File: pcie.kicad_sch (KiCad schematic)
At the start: 30 parts, among them J10 OCuLink_x4_Amphenol_G14A42121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, J11 OCuLink_x4_Amphenol_G14A42121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, J17 PinHeader_2x10_P1.27mm_SMD_Sh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

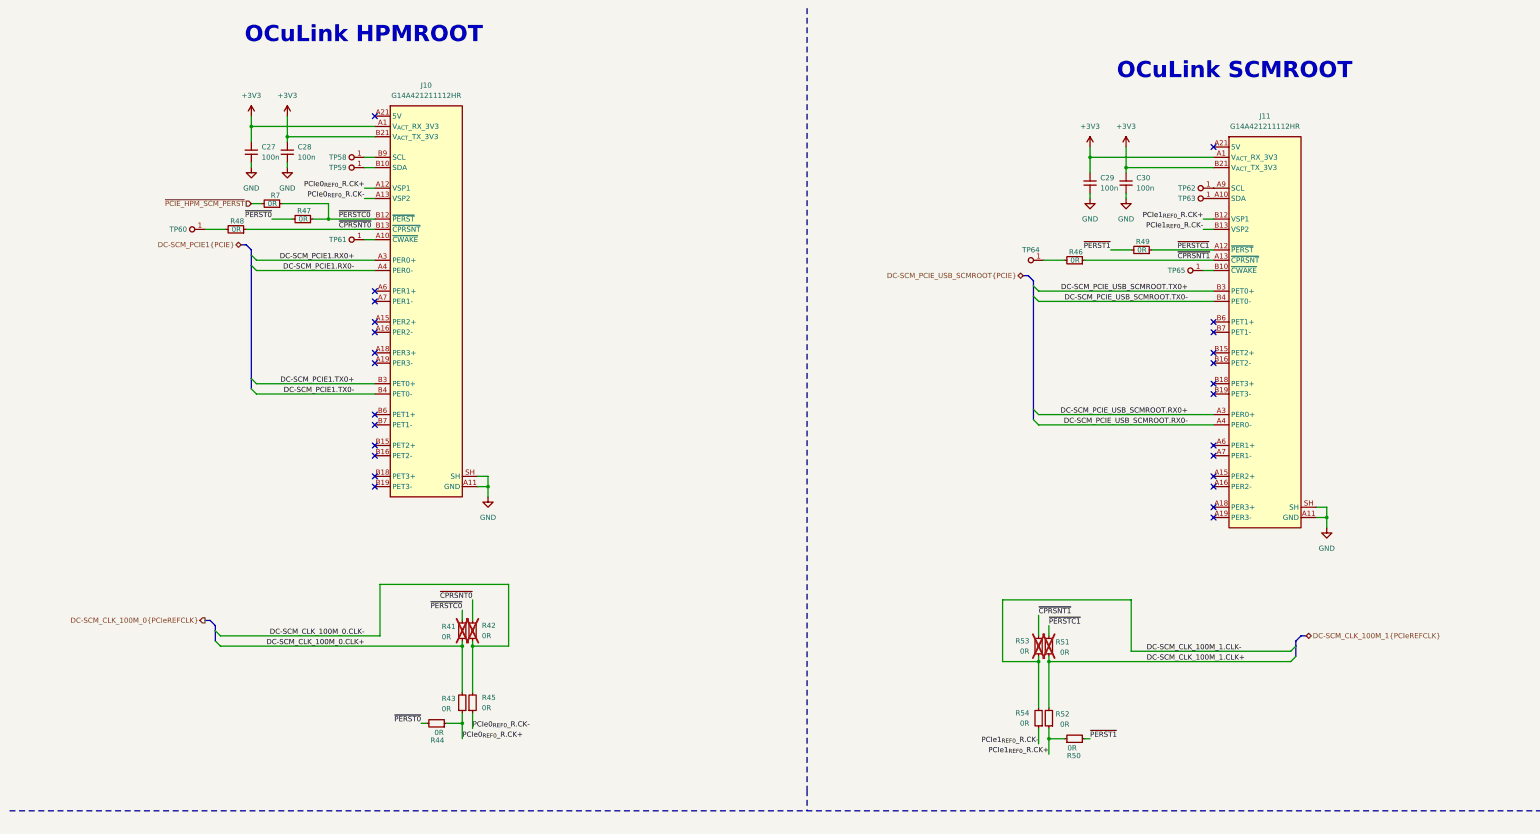
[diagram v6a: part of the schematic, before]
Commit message: [#93514] Add OCuLink Wiring and TVS diodes
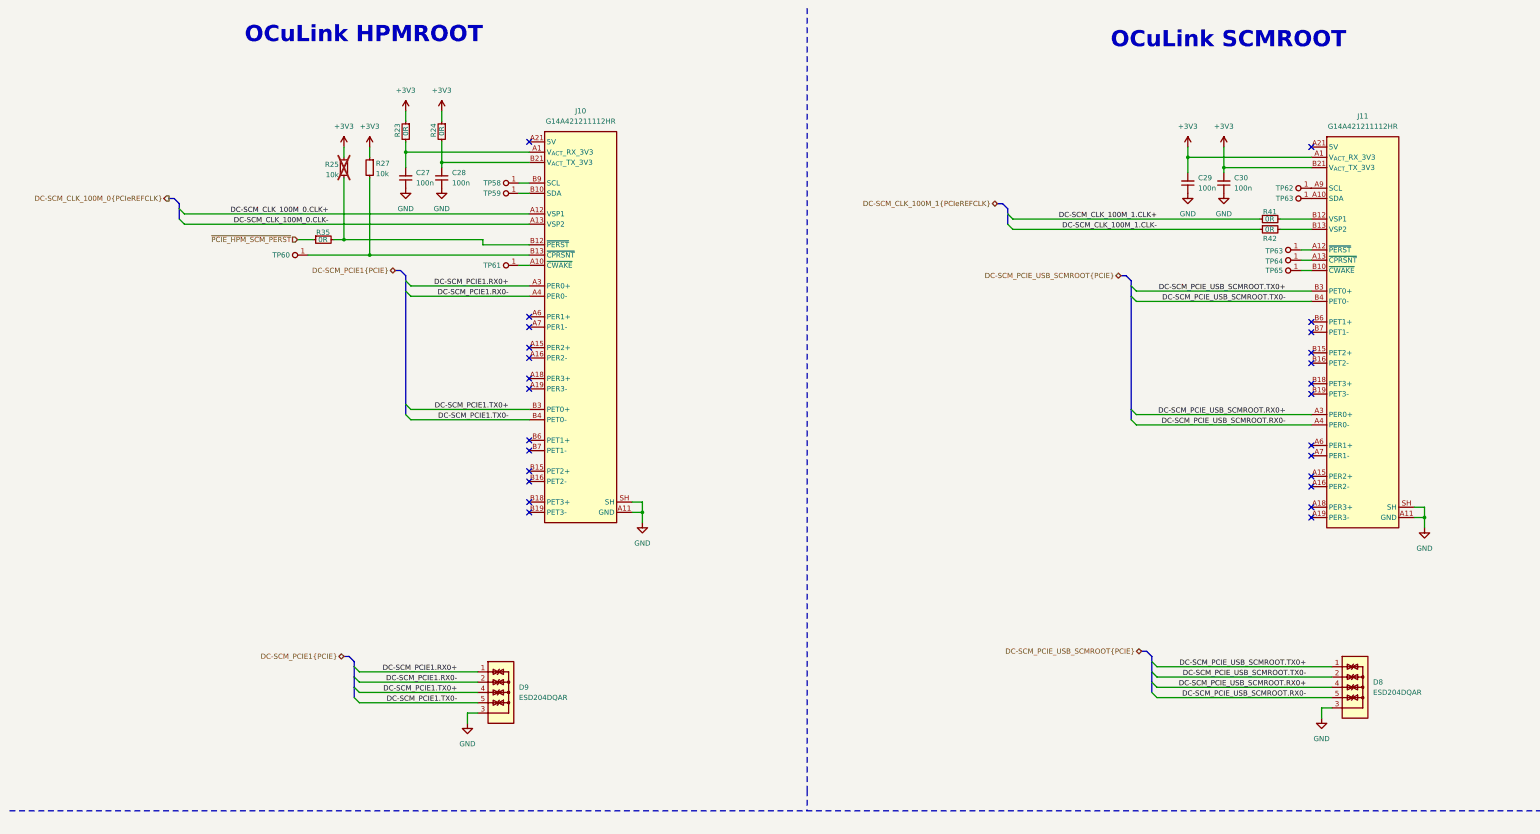
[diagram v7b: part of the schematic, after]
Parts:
- removed R43, R44, R45, R46, R47, R48, R49, R50, R51, R52, R53, R54, R7: R_0R_0402, antmicro-footprints:R_0402_1005Metric, symbol antmicroResistors0402:R_0R_0402
- added D8, D9: ESD204DQAR, antmicro-footprints:USON-10_2.5x1mm_P0.5mm, symbol antmicroTVSDiodes:ESD204DQAR
- added R23, R24, R35: R_0R_0402, antmicro-footprints:R_0402_1005Metric, symbol antmicroResistors0402:R_0R_0402
- added R25, R27: R_10k_0402, antmicro-footprints:R_0402_1005Metric, symbol antmicroResistors0402:R_10k_0402
- added TP63: TP_0.75mm_SMD, antmicro-footprints:TP_SMD_0.75mm, symbol antmicroTestPoints:TP_0.75mm_SMD
- R41, R42: now fitted
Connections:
- net PCIe0_{REF0}_R.CK+ is gone; now on net DC-SCM_CLK_100M_0.CLK+: J10.A12 (VSP1)
- net PCIe0_{REF0}_R.CK- is gone; now on net DC-SCM_CLK_100M_0.CLK-: J10.A13 (VSP2)
- net ~{CPRSNT1} is gone; now on an unnamed net: J11.A13 (~{CPRSNT})
- net +3V3: now also R23.1, R24.1, R25.1, R27.1; no longer C27.2, C28.2, J10.A1 (V_{ACT}_RX_3V3), J10.B21 (V_{ACT}_TX_3V3)
- net DC-SCM_CLK_100M_0.CLK+: no longer R41.1
- net DC-SCM_CLK_100M_0.CLK-: no longer R42.1
- net DC-SCM_CLK_100M_1.CLK+: now also R41.1
- net DC-SCM_CLK_100M_1.CLK-: now also R42.1
- net DC-SCM_PCIE1.RX0+: now also D9.1, D9.10
- net DC-SCM_PCIE1.RX0-: now also D9.2, D9.9
- net DC-SCM_PCIE1.TX0+: now also D9.4, D9.7
- net DC-SCM_PCIE1.TX0-: now also D9.5, D9.6
- net DC-SCM_PCIE_USB_SCMROOT.RX0+: now also D8.4, D8.7
- net DC-SCM_PCIE_USB_SCMROOT.RX0-: now also D8.5, D8.6
- net DC-SCM_PCIE_USB_SCMROOT.TX0+: now also D8.1, D8.10
- net DC-SCM_PCIE_USB_SCMROOT.TX0-: now also D8.2, D8.9
- net GND: now also D8.3, D8.8, D9.3, D9.8
- net ~{PCIE_HPM_SCM_PERST}: now also R35.1
- net at TP60.1: now also J10.B13 (~{CPRSNT}), R27.2
- net PCIe1_{REF0}_R.CK+: no longer names the net of J11.B12 (VSP1)
- net PCIe1_{REF0}_R.CK+: now also R41.2
- net PCIe1_{REF0}_R.CK-: no longer names the net of J11.B13 (VSP2)
- net PCIe1_{REF0}_R.CK-: now also R42.2
- removed net ~{CPRSNT0}: J10.B13 (~{CPRSNT}), R42.2
- net ~{PERSTC0}: no longer names the net of J10.B12 (~{PERST})
- net ~{PERSTC0}: now also R25.2, R35.2; no longer R41.2
- net ~{PERSTC1}: no longer names the net of J11.A12 (~{PERST})
- net ~{PERSTC1}: now also TP63.1
- new net: C28.2, J10.B21 (V_{ACT}_TX_3V3), R24.2
- new net: C27.2, J10.A1 (V_{ACT}_RX_3V3), R23.2
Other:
- moved on the sheet: C27, C28, C29, C30, J10, J11, TP58, TP59, TP60, TP61, TP62, TP63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

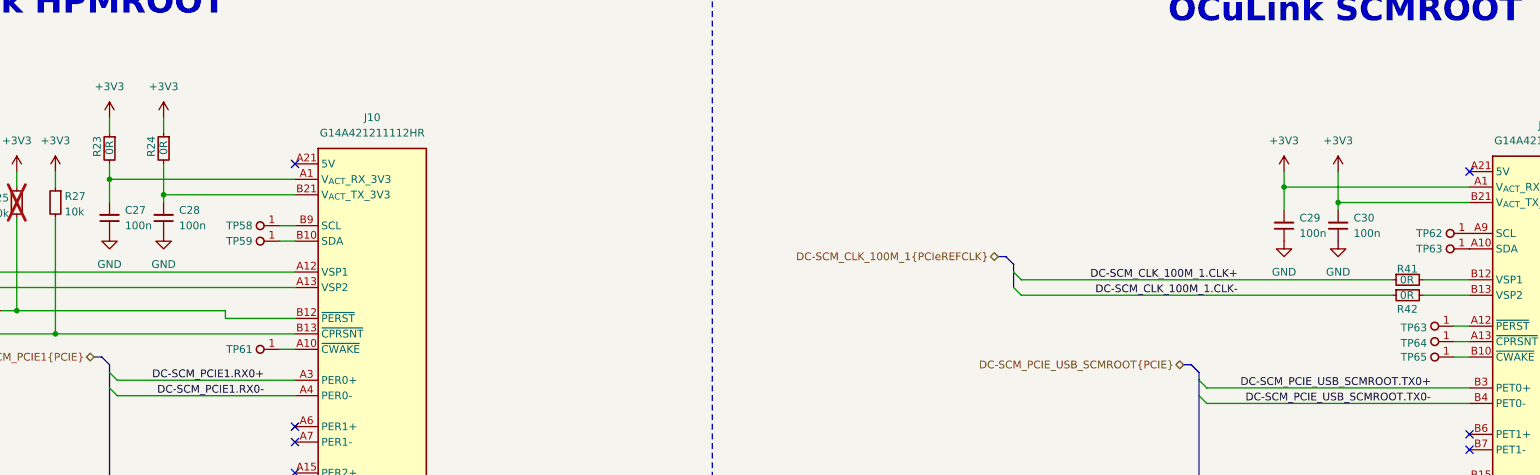
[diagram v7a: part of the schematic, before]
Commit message: [#93514] Remove duplicate components
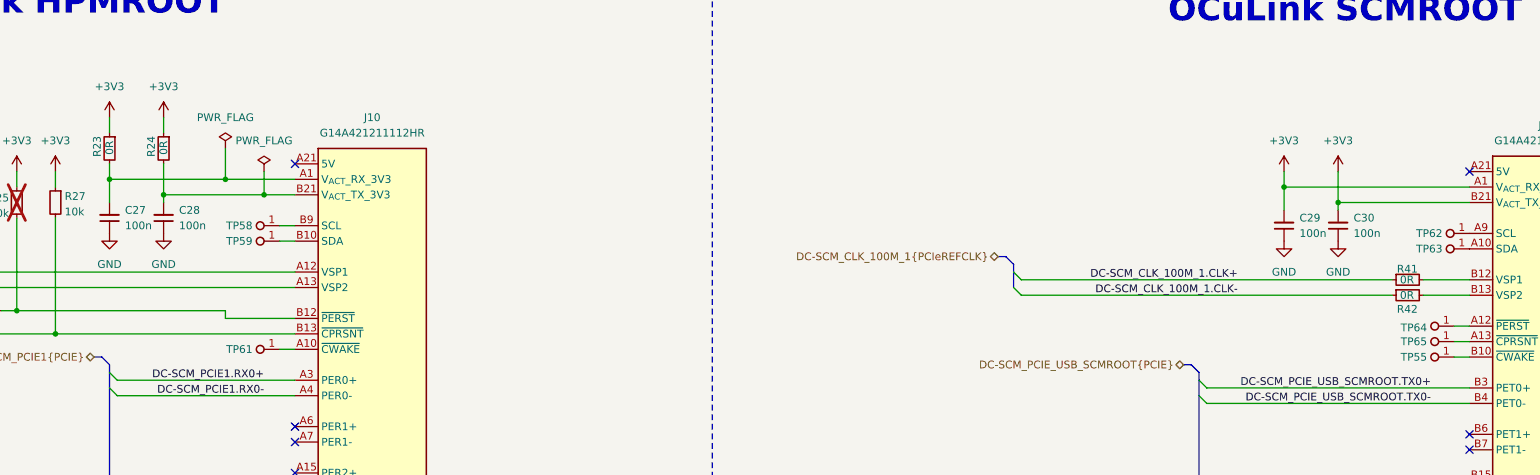
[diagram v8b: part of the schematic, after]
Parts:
- removed TP63: TP_0.75mm_SMD, antmicro-footprints:TP_SMD_0.75mm, symbol antmicroTestPoints:TP_0.75mm_SMD
- added TP55: TP_0.75mm_SMD, antmicro-footprints:TP_SMD_0.75mm, symbol antmicroTestPoints:TP_0.75mm_SMD
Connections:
- net at J11.A12 (~{PERST}): now also TP64.1
- net at J11.A13 (~{CPRSNT}): now also TP65.1; no longer TP64.1
- net at J11.B10 (~{CWAKE}): now also TP55.1; no longer TP65.1
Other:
- moved on the sheet: TP64, TP65
